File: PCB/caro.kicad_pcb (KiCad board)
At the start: 2 copper layers, 83.8 x 33 mm, 11 parts, among them SW1 Control Button, SW2 Power Switch, U1 DFR0299, U2 Arduino_Nano_v3.x

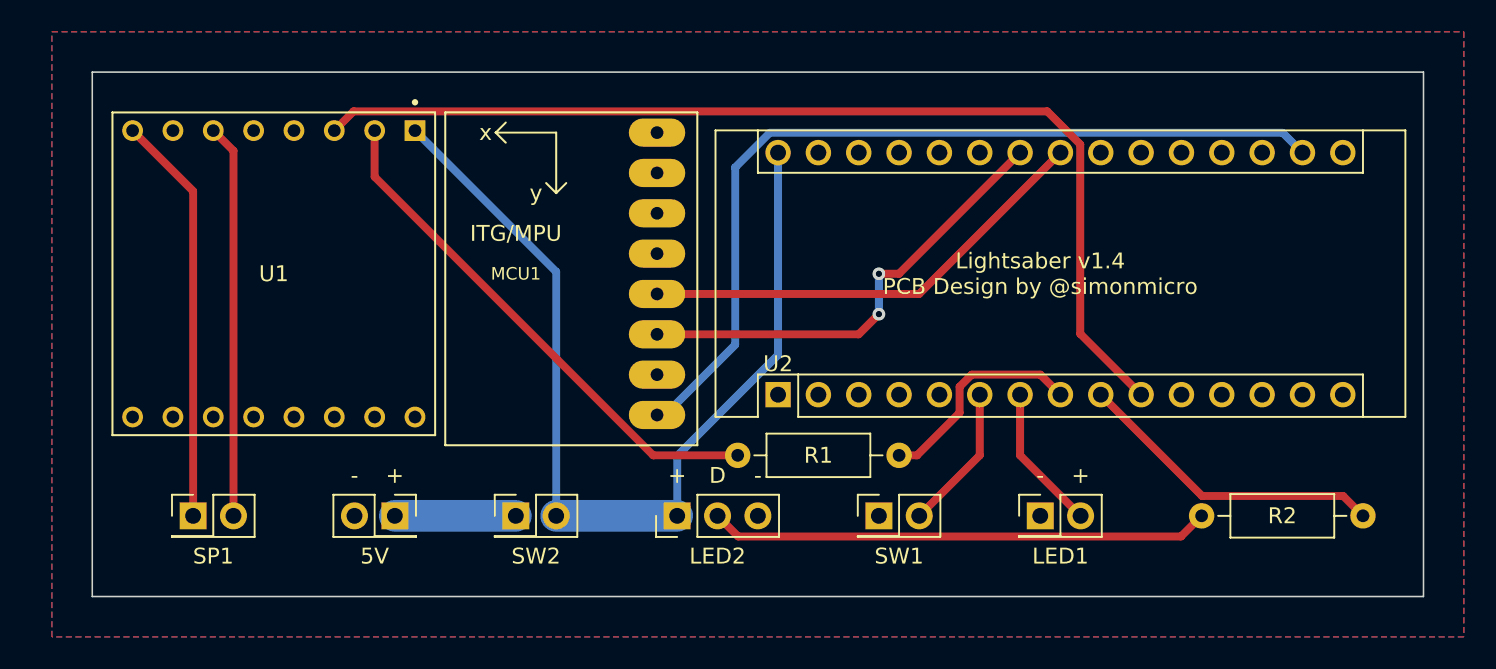
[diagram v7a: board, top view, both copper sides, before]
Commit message: Revision udate to v1.5 Swapped WS2812b to WS2811
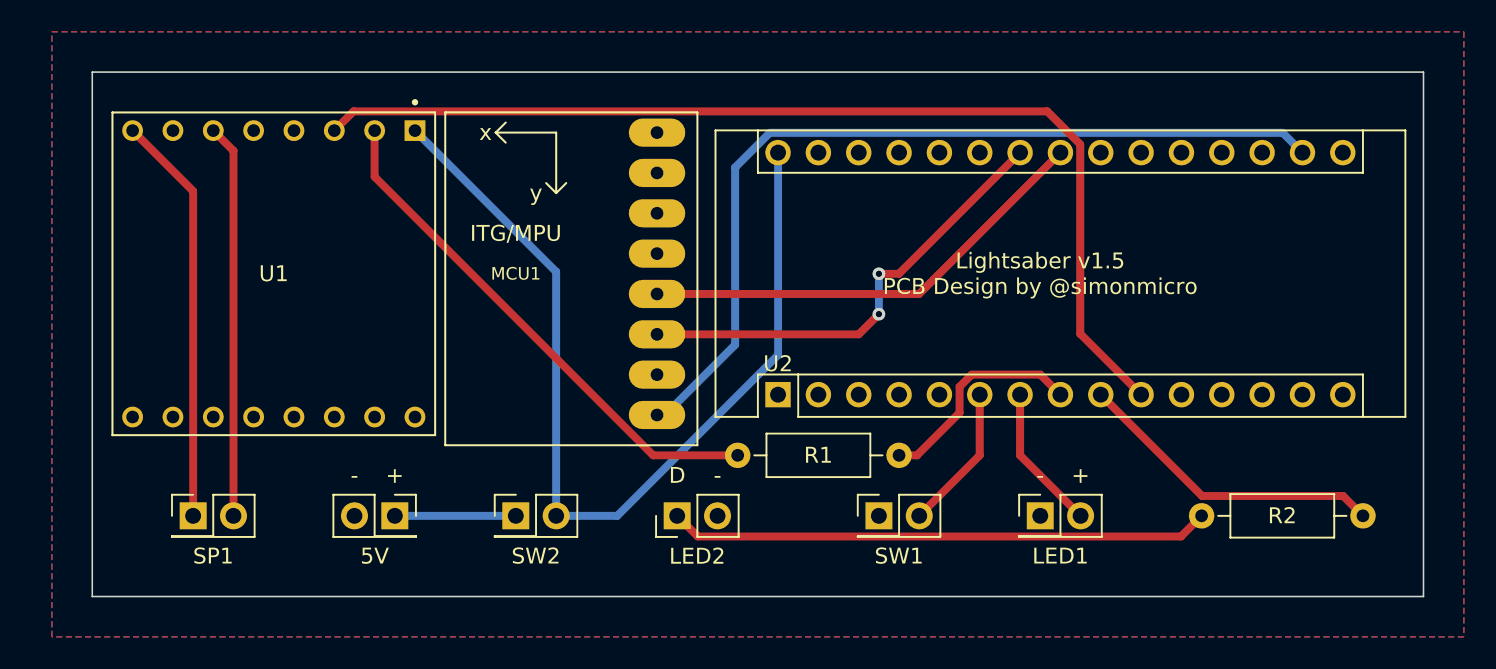
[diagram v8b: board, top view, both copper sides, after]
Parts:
- LED2: value WS2812B -> WS2811; footprint Connector_PinHeader_2.54mm:PinHeader_1x03_P2.54mm_Vertical -> Connector_PinHeader_2.54mm:PinHeader_1x02_P2.54mm_Vertical
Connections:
- LED2 pad 1: 5V -> Net-(R2-Pad2)
- R2 pad 2: Net-(LED2-Pad4) -> Net-(R2-Pad2)
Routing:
- net Net-(R2-Pad2): track 0.00 -> 34.1 mm
- net Net-(LED2-Pad4): track 31.6 -> 0.00 mm
- net 5V: track 61.1 -> 58.8 mm
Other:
- board text added: "Lightsaber v1.5 PCB Design by @simonmicro"
- board text removed: "Lightsaber v1.4 PCB Design by @simonmicro"
